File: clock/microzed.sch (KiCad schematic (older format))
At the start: 13 parts, among them U401 74LVC541

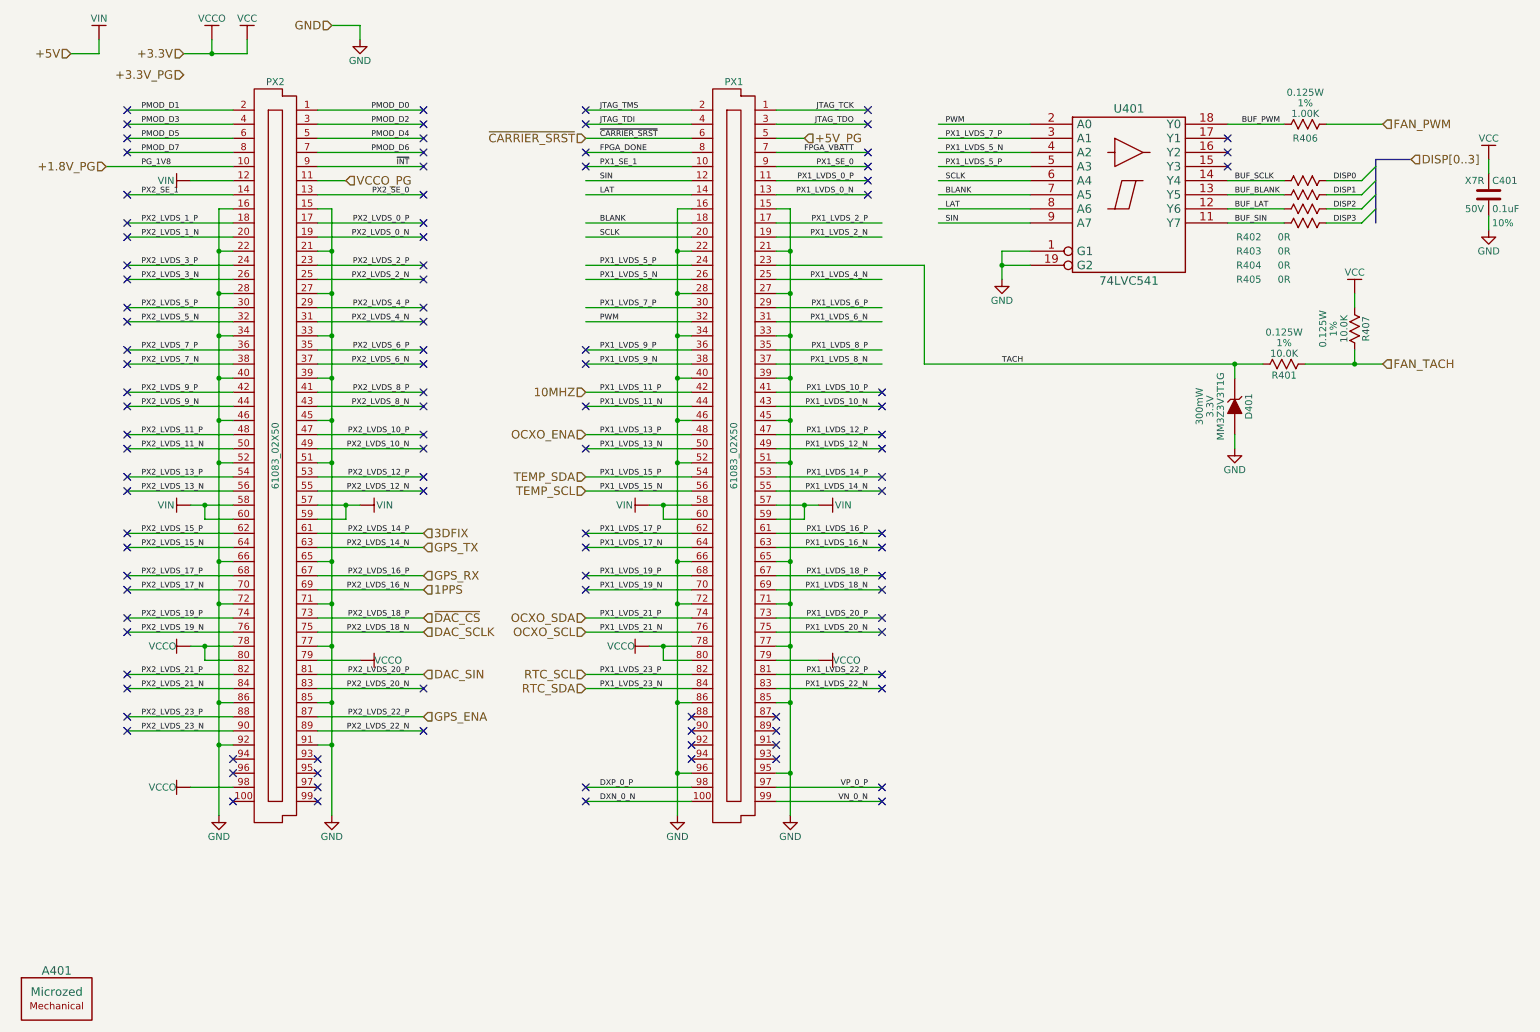
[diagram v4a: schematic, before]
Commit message: Add expansion connector, 8 GPIO pins and power.
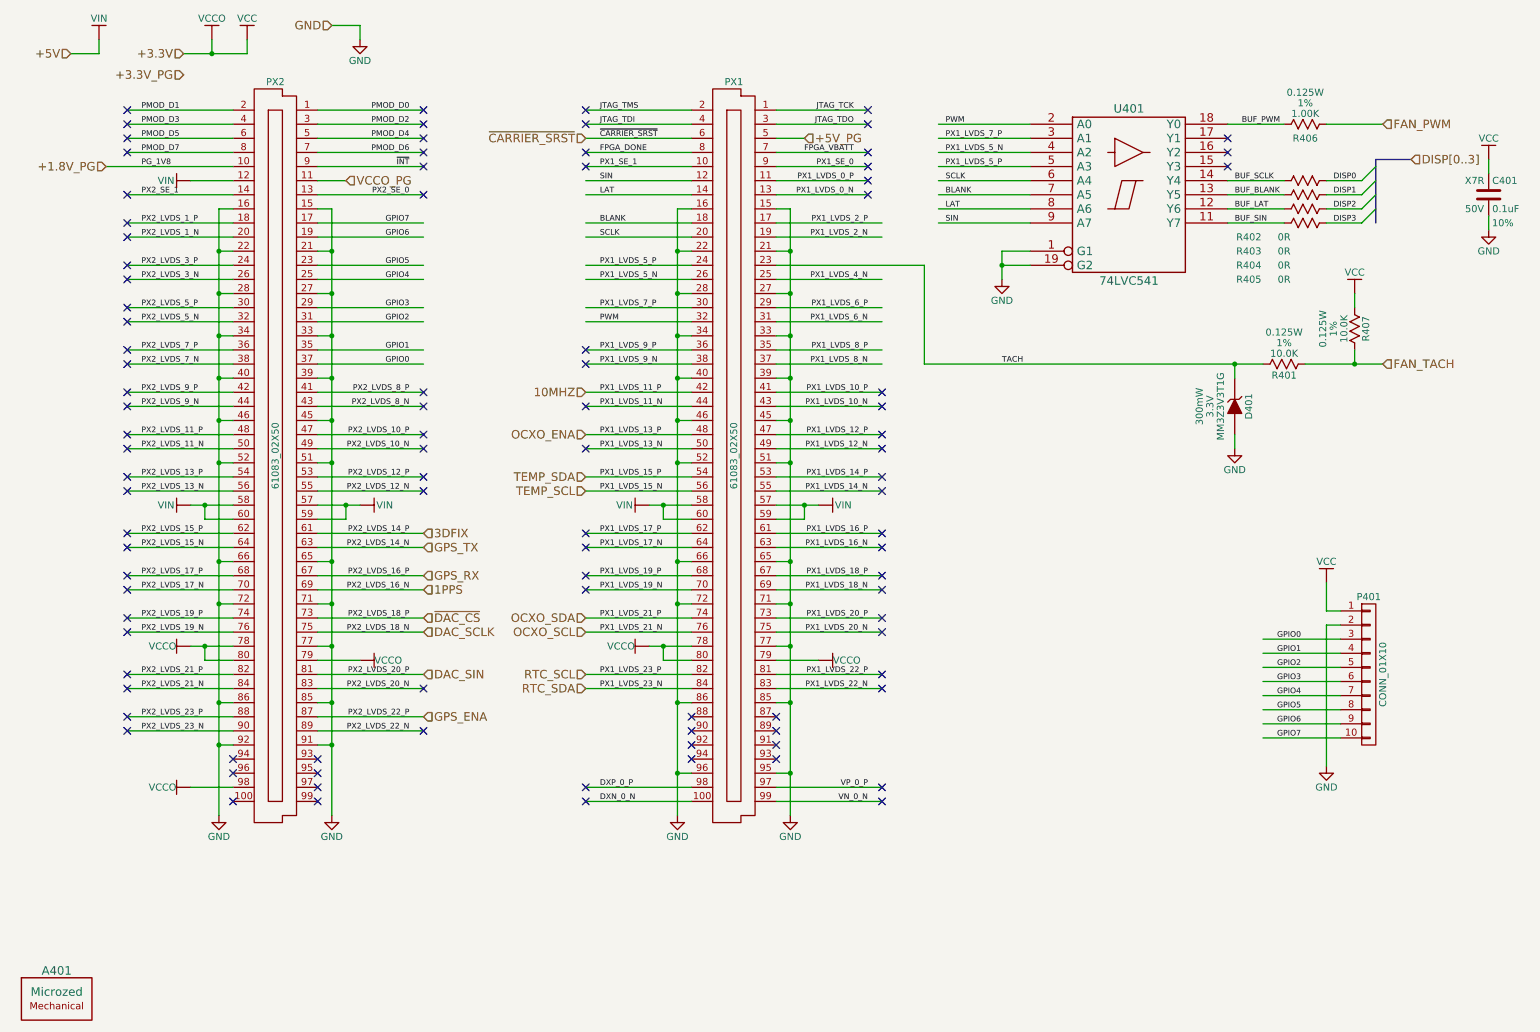
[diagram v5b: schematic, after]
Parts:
- added P401: CONN_01X10, Pin_Headers:Pin_Header_Angled_1x10, symbol CONN_01X10
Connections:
- net labels added: GPIO0, GPIO1, GPIO2, GPIO3, GPIO4, GPIO5, GPIO6, GPIO7
- net labels removed: PX2_LVDS_0_N, PX2_LVDS_0_P, PX2_LVDS_2_N, PX2_LVDS_2_P, PX2_LVDS_4_N, PX2_LVDS_4_P, PX2_LVDS_6_N, PX2_LVDS_6_P
- wire segments 232 -> 244
- no-connect marks 105 -> 97
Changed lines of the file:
@@
 Wire Wire Line
 	2650 2150 3400 2150
-Text Label 3300 2150 2    40   ~ 0
-PX2_LVDS_0_N
 NoConn ~ 1300 2750
 Wire Wire Line
 	2650 2050 3400 2050
-Text Label 3300 2050 2    40   ~ 0
-PX2_LVDS_0_P
 NoConn ~ 1300 2650
 Wire Wire Line
 	2650 2450 3400 2450
-Text Label 3300 2450 2    40   ~ 0
-PX2_LVDS_2_N
-NoConn ~ 3400 2450
 Wire Wire Line
 	2650 2350 3400 2350
-Text Label 3300 2350 2    40   ~ 0
-PX2_LVDS_2_P
 NoConn ~ 1300 2950
 Wire Wire Line
 	2650 2750 3400 2750
-Text Label 3300 2750 2    40   ~ 0
-PX2_LVDS_4_N
 NoConn ~ 1300 3950
 Wire Wire Line
 	2650 2650 3400 2650
-Text Label 3300 2650 2    40   ~ 0
-PX2_LVDS_4_P
 NoConn ~ 1300 3850
 Wire Wire Line
 	2650 3050 3400 3050
-Text Label 3300 3050 2    40   ~ 0
-PX2_LVDS_6_N
 NoConn ~ 1300 4350
 Wire Wire Line
 	2650 2950 3400 2950
-Text Label 3300 2950 2    40   ~ 0
-PX2_LVDS_6_P
 NoConn ~ 1300 4250
 Wire Wire Line
@@
 Text Label 3300 4350 2    40   ~ 0
 PX2_LVDS_14_N
-NoConn ~ 3400 2750
 Wire Wire Line
 	2650 4250 3400 4250
 Text Label 3300 4250 2    40   ~ 0
 PX2_LVDS_14_P
-NoConn ~ 3400 2650
 Text Label 1400 4550 0    40   ~ 0
 PX2_LVDS_17_P
@@
 Text Label 3300 4950 2    40   ~ 0
 PX2_LVDS_18_N
-NoConn ~ 3400 2150
 Wire Wire Line
 	2650 4850 3400 4850
 Text Label 3300 4850 2    40   ~ 0
 PX2_LVDS_18_P
-NoConn ~ 3400 2050
 Wire Wire Line
 	2650 5350 3400 5350
@@
 Text Label 3300 5250 2    40   ~ 0
 PX2_LVDS_20_P
-NoConn ~ 3400 2350
 Wire Wire Line
 	2650 5650 3400 5650
@@
 Text Label 4650 4550 0    40   ~ 0
 PX1_LVDS_19_P
-NoConn ~ 3400 2950
 Text Label 6550 4850 2    40   ~ 0
 PX1_LVDS_20_P
@@
 Text Label 4650 4950 0    40   ~ 0
 PX1_LVDS_21_N
-NoConn ~ 3400 3050
 Wire Wire Line
 	5300 4850 4550 4850
@@
 Text HLabel 4550 1450 0    60   Input ~ 0
 ~CARRIER_SRST~
+$Comp
+L CONN_01X10 P401
+U 1 1 569829DE
+P 10100 5250
+F 0 "P401" H 10100 5800 50  0000 C CNN
+F 1 "CONN_01X10" V 10200 5250 50  0000 C CNN
+F 2 "Pin_Headers:Pin_Header_Angled_1x10" H 10100 5250 50  0001 C CNN
+F 3 "" H 10100 5250 50  0000 C CNN
+	1    10100 5250
+	1    0    0    -1
+$EndComp
+Wire Wire Line
+	9900 4800 9800 4800
+Wire Wire Line
+	9800 4800 9800 4600
+$Comp
+L VCC #PWR069
+U 1 1 56982CA5
+P 9800 4600
+F 0 "#PWR069" H 9800 4450 50  0001 C CNN
+F 1 "VCC" H 9800 4750 50  0000 C CNN
+F 2 "" H 9800 4600 60  0000 C CNN
+F 3 "" H 9800 4600 60  0000 C CNN
+	1    9800 4600
+	1    0    0    -1
+$EndComp
+$Comp
+L GND #PWR070
+U 1 1 56982CDA
+P 9800 5900
+F 0 "#PWR070" H 9800 5650 50  0001 C CNN
+F 1 "GND" H 9800 5750 50  0000 C CNN
+F 2 "" H 9800 5900 60  0000 C CNN
+F 3 "" H 9800 5900 60  0000 C CNN
+	1    9800 5900
+	1    0    0    -1
+$EndComp
+Wire Wire Line
+	9800 5900 9800 4900
+Wire Wire Line
+	9800 4900 9900 4900
+Wire Wire Line
+	9900 5000 9350 5000
+Text Label 9450 5000 0    40   ~ 0
+GPIO0
+Wire Wire Line
+	9900 5100 9350 5100
+Text Label 9450 5100 0    40   ~ 0
+GPIO1
+Wire Wire Line
+	9900 5200 9350 5200
+Text Label 9450 5200 0    40   ~ 0
+GPIO2
+Wire Wire Line
+	9900 5300 9350 5300
+Text Label 9450 5300 0    40   ~ 0
+GPIO3
+Wire Wire Line
+	9900 5400 9350 5400
+Text Label 9450 5400 0    40   ~ 0
+GPIO4
+Wire Wire Line
+	9900 5500 9350 5500
+Text Label 9450 5500 0    40   ~ 0
+GPIO5
+Wire Wire Line
+	9900 5600 9350 5600
+Text Label 9450 5600 0    40   ~ 0
+GPIO6
+Wire Wire Line
+	9900 5700 9350 5700
+Text Label 9450 5700 0    40   ~ 0
+GPIO7
+Text Label 3300 3050 2    40   ~ 0
+GPIO0
+Text Label 3300 2950 2    40   ~ 0
+GPIO1
+Text Label 3300 2750 2    40   ~ 0
+GPIO2
+Text Label 3300 2650 2    40   ~ 0
+GPIO3
+Text Label 3300 2450 2    40   ~ 0
+GPIO4
+Text Label 3300 2350 2    40   ~ 0
+GPIO5
+Text Label 3300 2150 2    40   ~ 0
+GPIO6
+Text Label 3300 2050 2    40   ~ 0
+GPIO7
 $EndSCHEMATC

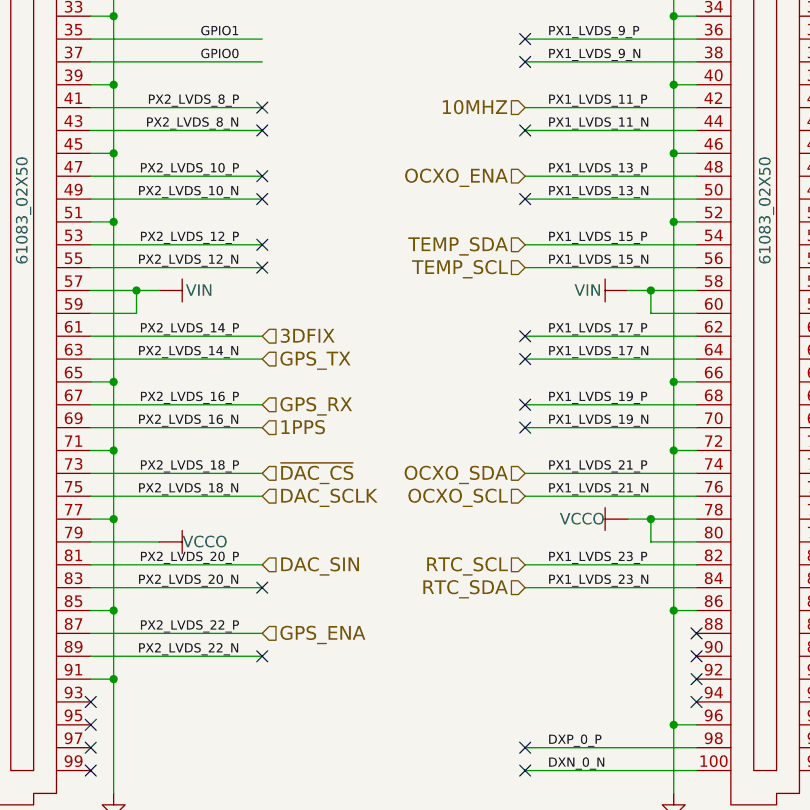
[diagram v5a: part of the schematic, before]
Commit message: Preliminary changes from lab bring up.   Properly connect ref2 on PCA9306.   Duplicate +5V power good to drive +3.3V converter.   Change gain structure on OCXO control voltage drive.   Add FET control to disable linear regulators.
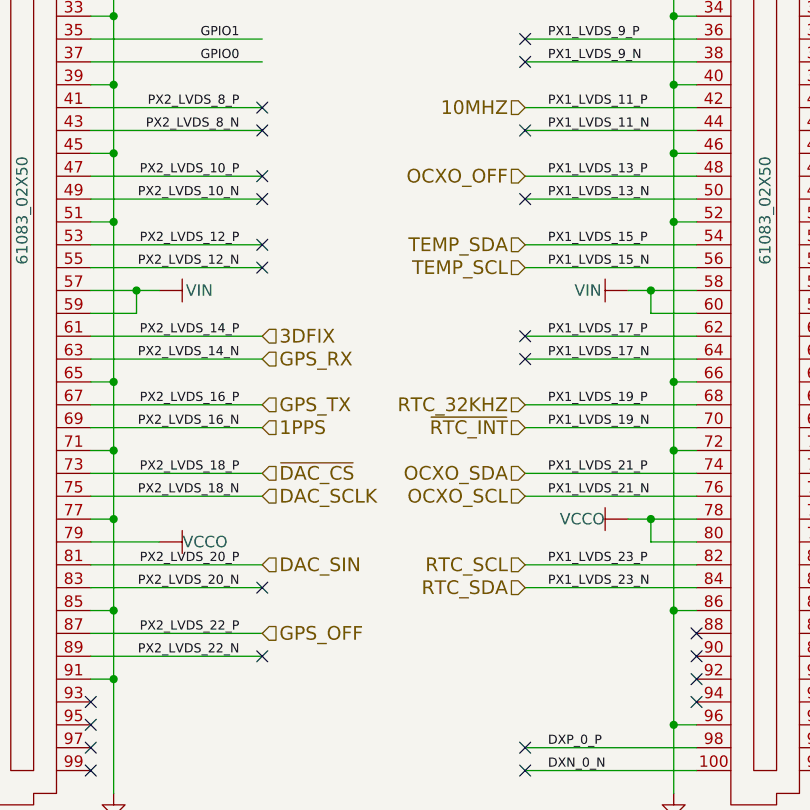
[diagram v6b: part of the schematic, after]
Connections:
- net labels added: GPS_OFF, OCXO_OFF, RTC_32KHZ, ~RTC_INT~
- net labels removed: GPS_ENA, OCXO_ENA
- no-connect marks 97 -> 95
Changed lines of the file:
@@
 $EndDescr
 $Comp
-L GND #PWR046
+L GND #PWR409
 U 1 1 5623DA38
 P 2750 6250
-F 0 "#PWR046" H 2750 6000 50  0001 C CNN
+F 0 "#PWR409" H 2750 6000 50  0001 C CNN
 F 1 "GND" H 2750 6100 50  0000 C CNN
 F 2 "" H 2750 6250 60  0000 C CNN
@@
 $EndComp
 $Comp
-L GND #PWR047
+L GND #PWR407
 U 1 1 5623DA70
 P 1950 6250
-F 0 "#PWR047" H 1950 6000 50  0001 C CNN
+F 0 "#PWR407" H 1950 6000 50  0001 C CNN
 F 1 "GND" H 1950 6100 50  0000 C CNN
 F 2 "" H 1950 6250 60  0000 C CNN
@@
 $EndComp
 $Comp
-L GND #PWR048
+L GND #PWR416
 U 1 1 5623DAE1
 P 6000 6250
-F 0 "#PWR048" H 6000 6000 50  0001 C CNN
+F 0 "#PWR416" H 6000 6000 50  0001 C CNN
 F 1 "GND" H 6000 6100 50  0000 C CNN
 F 2 "" H 6000 6250 60  0000 C CNN
@@
 $EndComp
 $Comp
-L GND #PWR049
+L GND #PWR415
 U 1 1 5623DB66
 P 5200 6250
-F 0 "#PWR049" H 5200 6000 50  0001 C CNN
+F 0 "#PWR415" H 5200 6000 50  0001 C CNN
 F 1 "GND" H 5200 6100 50  0000 C CNN
 F 2 "" H 5200 6250 60  0000 C CNN
@@
 	2050 1750 1750 1750
 $Comp
-L VIN #PWR050
+L VIN #PWR402
 U 1 1 5623ED14
 P 1750 1750
-F 0 "#PWR050" H 1750 1600 50  0001 C CNN
+F 0 "#PWR402" H 1750 1600 50  0001 C CNN
 F 1 "VIN" V 1750 1925 50  0000 C CNN
 F 2 "" H 1750 1750 60  0000 C CNN
@@
 $EndComp
 $Comp
-L VIN #PWR051
+L VIN #PWR403
 U 1 1 5623ED8A
 P 1750 4050
-F 0 "#PWR051" H 1750 3900 50  0001 C CNN
+F 0 "#PWR403" H 1750 3900 50  0001 C CNN
 F 1 "VIN" V 1750 4225 50  0000 C CNN
 F 2 "" H 1750 4050 60  0000 C CNN
@@
 $EndComp
 $Comp
-L VIN #PWR052
+L VIN #PWR411
 U 1 1 5623EE30
 P 2950 4050
-F 0 "#PWR052" H 2950 3900 50  0001 C CNN
+F 0 "#PWR411" H 2950 3900 50  0001 C CNN
 F 1 "VIN" V 2950 4225 50  0000 C CNN
 F 2 "" H 2950 4050 60  0000 C CNN
@@
 $EndComp
 $Comp
-L VIN #PWR053
+L VIN #PWR413
 U 1 1 5623EEAF
 P 5000 4050
-F 0 "#PWR053" H 5000 3900 50  0001 C CNN
+F 0 "#PWR413" H 5000 3900 50  0001 C CNN
 F 1 "VIN" V 5000 4225 50  0000 C CNN
 F 2 "" H 5000 4050 60  0000 C CNN
@@
 $EndComp
 $Comp
-L VIN #PWR054
+L VIN #PWR417
 U 1 1 5623EF12
 P 6200 4050
-F 0 "#PWR054" H 6200 3900 50  0001 C CNN
+F 0 "#PWR417" H 6200 3900 50  0001 C CNN
 F 1 "VIN" V 6200 4225 50  0000 C CNN
 F 2 "" H 6200 4050 60  0000 C CNN
@@
 Connection ~ 5100 5050
 $Comp
-L VCCO #PWR055
+L VCCO #PWR418
 U 1 1 5623F518
 P 6200 5150
-F 0 "#PWR055" H 6200 5000 50  0001 C CNN
+F 0 "#PWR418" H 6200 5000 50  0001 C CNN
 F 1 "VCCO" V 6200 5350 50  0000 C CNN
 F 2 "" H 6200 5150 60  0000 C CNN
@@
 Connection ~ 1850 5050
 $Comp
-L VCCO #PWR056
+L VCCO #PWR404
 U 1 1 5623F63E
 P 1750 5050
-F 0 "#PWR056" H 1750 4900 50  0001 C CNN
+F 0 "#PWR404" H 1750 4900 50  0001 C CNN
 F 1 "VCCO" V 1750 5250 50  0000 C CNN
 F 2 "" H 1750 5050 60  0000 C CNN
@@
 	2650 5150 2950 5150
 $Comp
-L VCCO #PWR057
+L VCCO #PWR412
 U 1 1 5623F67B
 P 2950 5150
-F 0 "#PWR057" H 2950 5000 50  0001 C CNN
+F 0 "#PWR412" H 2950 5000 50  0001 C CNN
 F 1 "VCCO" V 2950 5350 50  0000 C CNN
 F 2 "" H 2950 5150 60  0000 C CNN
@@
 	2050 6050 1750 6050
 $Comp
-L VCCO #PWR058
+L VCCO #PWR405
 U 1 1 5623F755
 P 1750 6050
-F 0 "#PWR058" H 1750 5900 50  0001 C CNN
+F 0 "#PWR405" H 1750 5900 50  0001 C CNN
 F 1 "VCCO" V 1750 6250 50  0000 C CNN
 F 2 "" H 1750 6050 60  0000 C CNN
@@
 VCCO_PG
 Text HLabel 3400 4350 2    60   Input ~ 0
+GPS_RX
+Text HLabel 3400 4550 2    60   Input ~ 0
 GPS_TX
-Text HLabel 3400 4550 2    60   Input ~ 0
-GPS_RX
 Text HLabel 4550 4950 0    60   Input ~ 0
 OCXO_SCL
@@
 DAC_SIN
 Text HLabel 3400 5550 2    60   Input ~ 0
-GPS_ENA
+GPS_OFF
 Text HLabel 4550 3550 0    60   Input ~ 0
-OCXO_ENA
+OCXO_OFF
 Text HLabel 4550 3250 0    60   Input ~ 0
 10MHZ
@@
 3DFIX
 $Comp
-L VIN #PWR059
+L VIN #PWR401
 U 1 1 562597FE
 P 1100 750
-F 0 "#PWR059" H 1100 600 50  0001 C CNN
+F 0 "#PWR401" H 1100 600 50  0001 C CNN
 F 1 "VIN" H 1100 900 50  0000 C CNN
 F 2 "" H 1100 750 60  0000 C CNN
@@
 	1100 850  1100 750
 $Comp
-L VCCO #PWR060
+L VCCO #PWR406
 U 1 1 562598AE
 P 1900 750
-F 0 "#PWR060" H 1900 600 50  0001 C CNN
+F 0 "#PWR406" H 1900 600 50  0001 C CNN
 F 1 "VCCO" H 1900 900 50  0000 C CNN
 F 2 "" H 1900 750 60  0000 C CNN
@@
 	1900 850  1900 750
 $Comp
-L GND #PWR061
+L GND #PWR410
 U 1 1 56259970
 P 2950 750
-F 0 "#PWR061" H 2950 500 50  0001 C CNN
+F 0 "#PWR410" H 2950 500 50  0001 C CNN
 F 1 "GND" H 2950 600 50  0000 C CNN
 F 2 "" H 2950 750 60  0000 C CNN
@@
 DISP3
 $Comp
-L VCC #PWR062
+L VCC #PWR408
 U 1 1 56368B50
 P 2150 750
-F 0 "#PWR062" H 2150 600 50  0001 C CNN
+F 0 "#PWR408" H 2150 600 50  0001 C CNN
 F 1 "VCC" H 2150 900 50  0000 C CNN
 F 2 "" H 2150 750 60  0000 C CNN
@@
 Connection ~ 7500 2350
 $Comp
-L GND #PWR063
+L GND #PWR419
 U 1 1 56369E58
 P 7500 2450
-F 0 "#PWR063" H 7500 2200 50  0001 C CNN
+F 0 "#PWR419" H 7500 2200 50  0001 C CNN
 F 1 "GND" H 7500 2300 50  0000 C CNN
 F 2 "" H 7500 2450 60  0000 C CNN
@@
 	9150 3050 9150 3150
 $Comp
-L VCC #PWR064
+L VCC #PWR423
 U 1 1 563911B0
 P 10000 2550
-F 0 "#PWR064" H 10000 2400 50  0001 C CNN
+F 0 "#PWR423" H 10000 2400 50  0001 C CNN
 F 1 "VCC" H 10000 2700 50  0000 C CNN
 F 2 "" H 10000 2550 60  0000 C CNN
@@
 $EndComp
 $Comp
-L GND #PWR065
+L GND #PWR420
 U 1 1 563911DC
 P 9150 3650
-F 0 "#PWR065" H 9150 3400 50  0001 C CNN
+F 0 "#PWR420" H 9150 3400 50  0001 C CNN
 F 1 "GND" H 9150 3500 50  0000 C CNN
 F 2 "" H 9150 3650 60  0000 C CNN
@@
 NoConn ~ 9100 1650
 $Comp
-L VCCO #PWR066
+L VCCO #PWR414
 U 1 1 563E2413
 P 5000 5050
-F 0 "#PWR066" H 5000 4900 50  0001 C CNN
+F 0 "#PWR414" H 5000 4900 50  0001 C CNN
 F 1 "VCCO" V 5000 5250 50  0000 C CNN
 F 2 "" H 5000 5050 60  0000 C CNN
@@
 TACH
 $Comp
-L GND #PWR067
+L GND #PWR425
 U 1 1 56403C33
 P 10950 2100
-F 0 "#PWR067" H 10950 1850 50  0001 C CNN
+F 0 "#PWR425" H 10950 1850 50  0001 C CNN
 F 1 "GND" H 10950 1950 50  0000 C CNN
 F 2 "" H 10950 2100 60  0000 C CNN
@@
 $EndComp
 $Comp
-L VCC #PWR068
+L VCC #PWR424
 U 1 1 56403C47
 P 10950 1600
-F 0 "#PWR068" H 10950 1450 50  0001 C CNN
+F 0 "#PWR424" H 10950 1450 50  0001 C CNN
 F 1 "VCC" H 10950 1750 50  0000 C CNN
 F 2 "" H 10950 1600 60  0000 C CNN
@@
 Text Label 4650 4650 0    40   ~ 0
 PX1_LVDS_19_N
-NoConn ~ 4550 4650
 Wire Wire Line
 	5300 4550 4550 4550
@@
 Text Label 4650 4850 0    40   ~ 0
 PX1_LVDS_21_P
-NoConn ~ 4550 4550
 Wire Wire Line
 	5300 5350 4550 5350
@@
 	9800 4800 9800 4600
 $Comp
-L VCC #PWR069
+L VCC #PWR421
 U 1 1 56982CA5
 P 9800 4600
-F 0 "#PWR069" H 9800 4450 50  0001 C CNN
+F 0 "#PWR421" H 9800 4450 50  0001 C CNN
 F 1 "VCC" H 9800 4750 50  0000 C CNN
 F 2 "" H 9800 4600 60  0000 C CNN
@@
 $EndComp
 $Comp
-L GND #PWR070
+L GND #PWR422
 U 1 1 56982CDA
 P 9800 5900
-F 0 "#PWR070" H 9800 5650 50  0001 C CNN
+F 0 "#PWR422" H 9800 5650 50  0001 C CNN
 F 1 "GND" H 9800 5750 50  0000 C CNN
 F 2 "" H 9800 5900 60  0000 C CNN
@@
 Text Label 3300 2050 2    40   ~ 0
 GPIO7
+Text HLabel 4550 4550 0    60   Input ~ 0
+RTC_32KHZ
+Text HLabel 4550 4650 0    60   Input ~ 0
+~RTC_INT~
 $EndSCHEMATC
